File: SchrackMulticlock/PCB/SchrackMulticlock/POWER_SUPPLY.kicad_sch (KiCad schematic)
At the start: 7 parts, among them SW1 SW_SPST, U1 LM1084-3.3

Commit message: Stopwatch.h + Schematic update
Multiclock Scheamtic and code update
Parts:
- BT1: footprint Schrack_brd:SOLDER_PADS -> Battery:BatteryHolder_TruPower_BH-331P_3xAA
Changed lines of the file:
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@@
 			)
 		)
-		(property "Footprint" "Schrack_brd:SOLDER_PADS"
+		(property "Footprint" "Battery:BatteryHolder_TruPower_BH-331P_3xAA"
 			(at 125.73 122.936 90)
 			(effects

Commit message: schrack multiclock schematic update
Just regular updates
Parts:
- removed C1, C4: 10uF, Capacitor_Tantalum_SMD:CP_EIA-3216-18_Kemet-A_Pad1.58x1.35mm_HandSolder, symbol Device:C_Polarized
- removed U1: LM1084-3.3, Package_TO_SOT_SMD:TO-263-3_TabPin2, symbol Regulator_Linear:LM1084-3.3
- added C? (x2): 10uF, Capacitor_Tantalum_SMD:CP_EIA-3216-18_Kemet-A_Pad1.58x1.35mm_HandSolder, symbol Device:C_Polarized
- added U?: LM1117DT-3.3, Package_TO_SOT_SMD:TO-252-3_TabPin2, symbol Regulator_Linear:LM1117DT-3.3
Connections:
- net +3V3: now also C?.1, U?.2 (VO)
- net +5V: now also C?.1, U?.3 (VI)
- net GND: now also C?.2, C?.2, U?.1 (GND)

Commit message: SchrackMulticlock schematic
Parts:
- gave numbers to parts that had none: 3
- renumbered C2 to C1
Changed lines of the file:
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@@
 		(dnp no)
 		(fields_autoplaced yes)
-		(property "Reference" "#PWR01"
+		(property "Reference" "#PWR0102"
 			(at 92.71 132.08 0)
 			(effects
@@
 			(project "SchrackCounter"
 				(path "/d96f2ffc-3f4c-4f71-b693-29f6b8c3245d/2b0bd697-1473-4a31-8990-1278f12dea07"
-					(reference "#PWR01")
+					(reference "#PWR0102")
 					(unit 1)
 				)
@@
 		(on_board yes)
 		(dnp no)
-		(property "Reference" "C2"
+		(property "Reference" "C1"
 			(at 106.68 123.825 0)
 			(effects
@@
 			(project "SchrackCounter"
 				(path "/d96f2ffc-3f4c-4f71-b693-29f6b8c3245d/2b0bd697-1473-4a31-8990-1278f12dea07"
-					(reference "C2")
+					(reference "C1")
 					(unit 1)
 				)
@@
 		(dnp no)
 		(fields_autoplaced yes)
-		(property "Reference" "U?"
+		(property "Reference" "U1"
 			(at 118.11 53.34 0)
 			(effects
@@
 			(project "SchrackMulticlock"
 				(path "/d96f2ffc-3f4c-4f71-b693-29f6b8c3245d/2b0bd697-1473-4a31-8990-1278f12dea07"
-					(reference "U?")
+					(reference "U1")
 					(unit 1)
 				)
@@
 		(on_board yes)
 		(dnp no)
-		(property "Reference" "C?"
+		(property "Reference" "C4"
 			(at 132.715 65.405 0)
 			(effects
@@
 			(project "SchrackMulticlock"
 				(path "/d96f2ffc-3f4c-4f71-b693-29f6b8c3245d/2b0bd697-1473-4a31-8990-1278f12dea07"
-					(reference "C?")
+					(reference "C4")
 					(unit 1)
 				)
@@
 		(on_board yes)
 		(dnp no)
-		(property "Reference" "C?"
+		(property "Reference" "C2"
 			(at 100.33 65.405 0)
 			(effects
@@
 			(project "SchrackMulticlock"
 				(path "/d96f2ffc-3f4c-4f71-b693-29f6b8c3245d/2b0bd697-1473-4a31-8990-1278f12dea07"
-					(reference "C?")
+					(reference "C2")
 					(unit 1)
 				)
@@
 		(on_board yes)
 		(dnp no)
-		(property "Reference" "#PWR02"
+		(property "Reference" "#PWR0101"
 			(at 106.68 59.69 0)
 			(effects
@@
 			(project "SchrackMulticlock"
 				(path "/d96f2ffc-3f4c-4f71-b693-29f6b8c3245d/2b0bd697-1473-4a31-8990-1278f12dea07"
-					(reference "#PWR02")
+					(reference "#PWR0101")
 					(unit 1)
 				)
@@
 		(on_board yes)
 		(dnp no)
-		(property "Reference" "#PWR03"
+		(property "Reference" "#PWR0103"
 			(at 118.11 82.55 0)
 			(effects
@@
 			(project "SchrackMulticlock"
 				(path "/d96f2ffc-3f4c-4f71-b693-29f6b8c3245d/2b0bd697-1473-4a31-8990-1278f12dea07"
-					(reference "#PWR03")
+					(reference "#PWR0103")
 					(unit 1)
 				)
@@
 		(on_board yes)
 		(dnp no)
-		(property "Reference" "#PWR05"
+		(property "Reference" "#PWR0105"
 			(at 185.42 68.58 0)
 			(effects
@@
 			(project "SchrackCounter"
 				(path "/d96f2ffc-3f4c-4f71-b693-29f6b8c3245d/2b0bd697-1473-4a31-8990-1278f12dea07"
-					(reference "#PWR05")
+					(reference "#PWR0105")
 					(unit 1)
 				)
@@
 		(on_board yes)
 		(dnp no)
-		(property "Reference" "#PWR04"
+		(property "Reference" "#PWR0104"
 			(at 128.27 59.69 0)
 			(effects
@@
 			(project "SchrackMulticlock"
 				(path "/d96f2ffc-3f4c-4f71-b693-29f6b8c3245d/2b0bd697-1473-4a31-8990-1278f12dea07"
-					(reference "#PWR04")
-					(unit 1)
-				)
+					(reference "#PWR0104")
+					(unit 1)
+				)

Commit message: Multiclock pcb update
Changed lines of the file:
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@@
 	(text "Texas Instruments \nLDO Voltage Regulator\n\nLM1084IS-3.3/NOPB 3.3V\n\nUsing TO-263-3 footprint"
 		(exclude_from_sim no)
-		(at 77.47 32.385 0)
+		(at 34.925 67.31 0)
 		(effects
 			(font

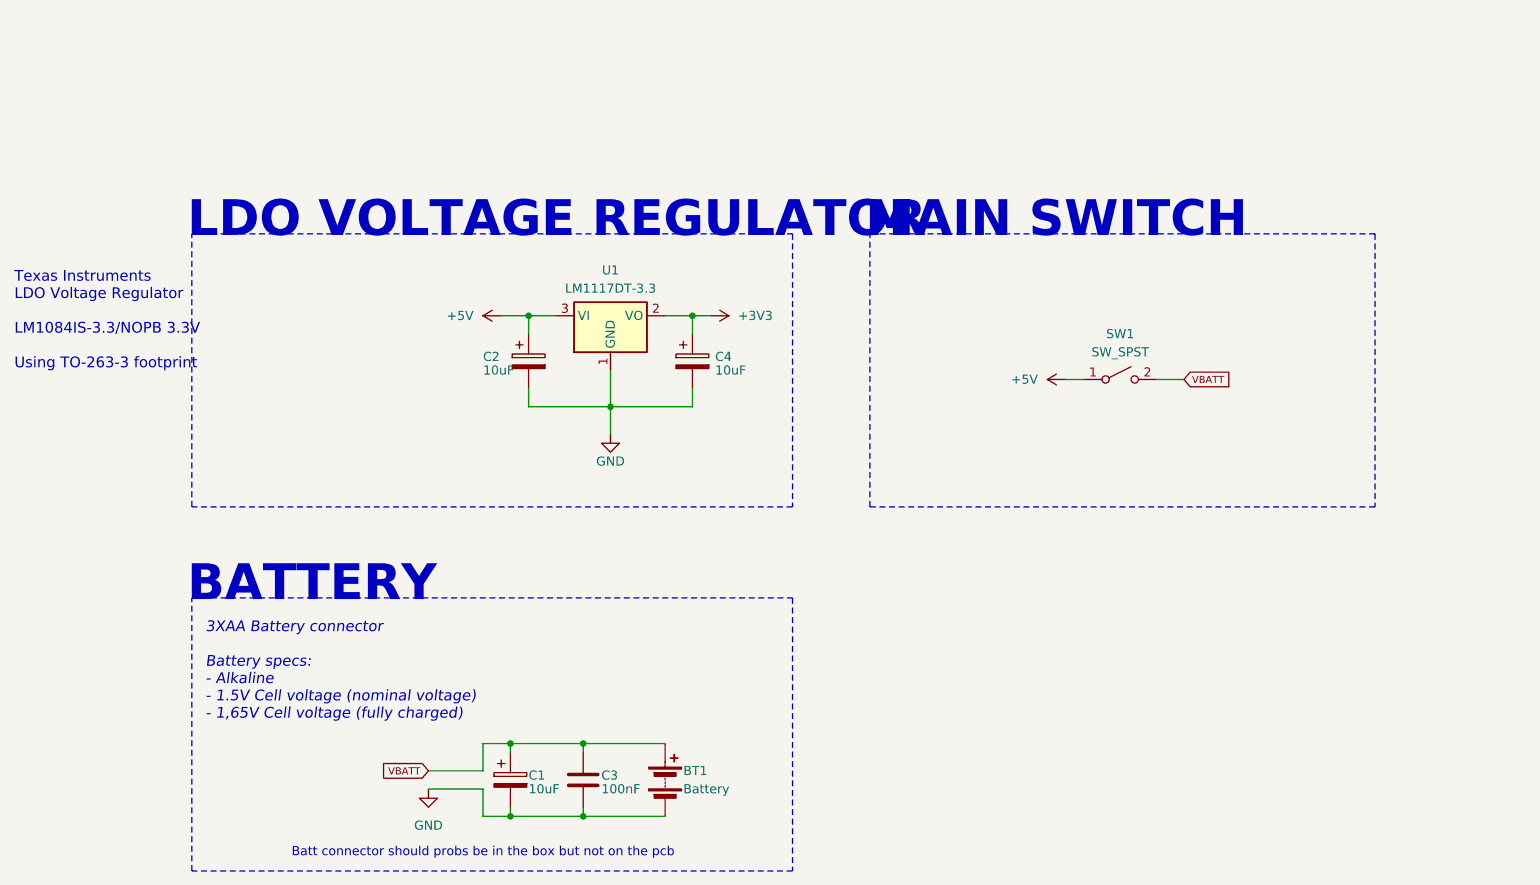
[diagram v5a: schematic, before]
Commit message: SchrackMulticlock and Counter pcb updates
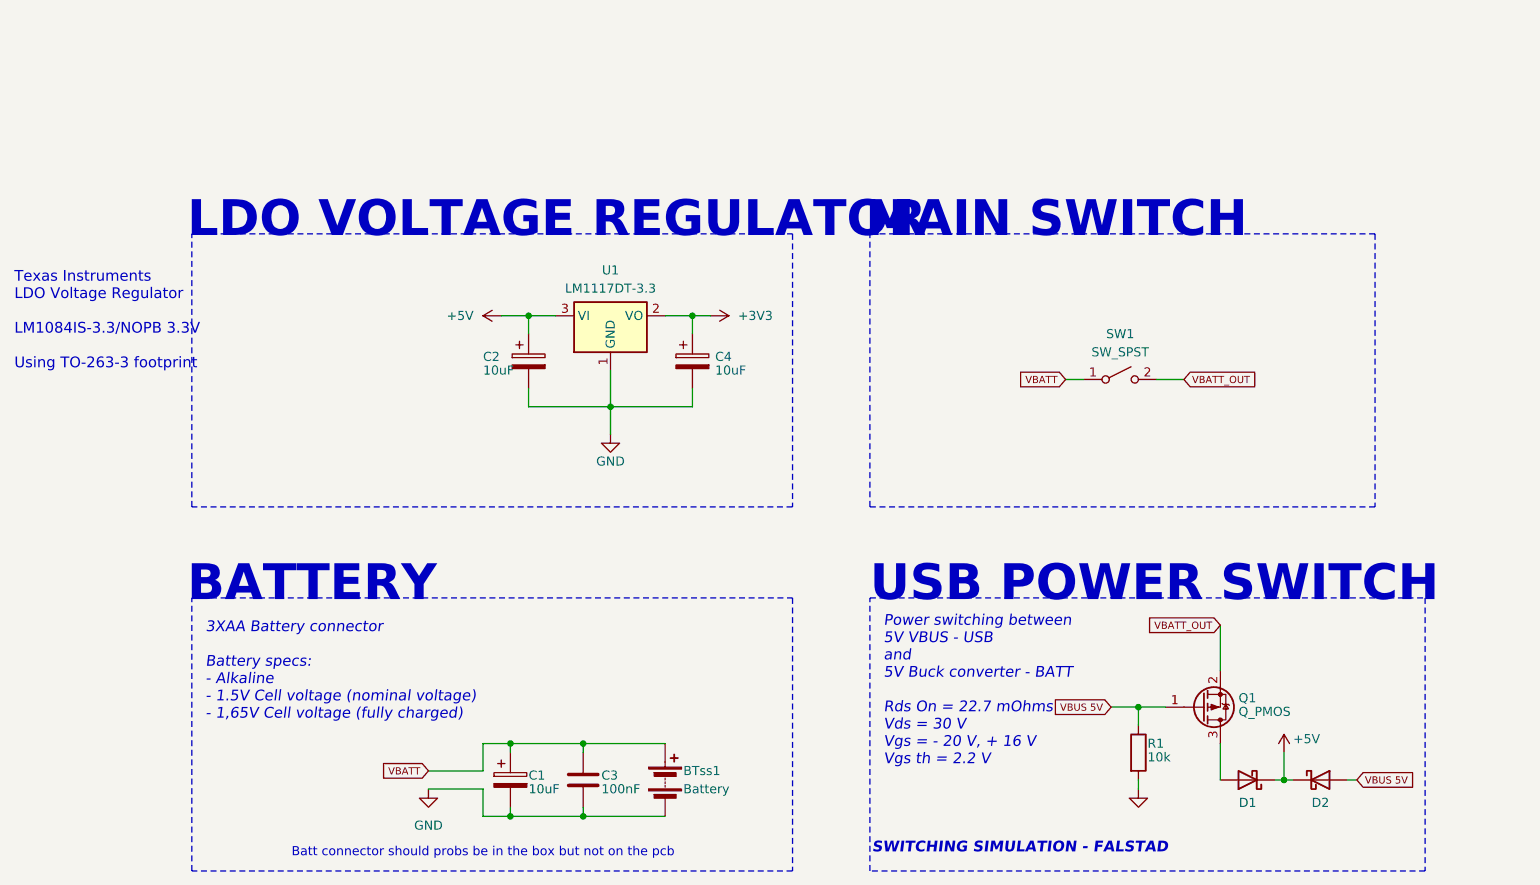
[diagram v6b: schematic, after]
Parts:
- added D1, D2: D_Schottky, Diode_SMD:D_1206_3216Metric_Pad1.42x1.75mm_HandSolder, symbol Device:D_Schottky
- added Q1: Q_PMOS, Package_TO_SOT_SMD:SOT-23-3, symbol Device:Q_PMOS_GSD
- added R1: 10k, Resistor_SMD:R_0805_2012Metric_Pad1.20x1.40mm_HandSolder, symbol Device:R
- BTss1: renamed from BT1; footprint Battery:BatteryHolder_TruPower_BH-331P_3xAA -> Schrack_brd:SOLDER_PADS
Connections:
- net +5V: now also D1.1 (K), D2.1 (K); no longer SW1.1 (A)
- net GND: now also R1.2
- net VBATT: now also SW1.1 (A); no longer SW1.2 (B)
- new net: D1.2 (A), Q1.3 (D)
- new net VBATT_OUT: Q1.2 (S), SW1.2 (B)
- new net VBUS 5V: D2.2 (A), Q1.1 (G), R1.1
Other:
- note added: "Power switching between 5V VBUS - USB and 5V Buck converter - BATT"
- note added: "Rds On = 22.7 mOhms Vds = 30 V Vgs = - 20 V, + 16 V Vgs th = 2.2 V"
- note added: "SWITCHING SIMULATION - FALSTAD"
- note added: "USB POWER SWITCH"
